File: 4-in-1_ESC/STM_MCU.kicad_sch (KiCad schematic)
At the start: 4 parts, among them U9 STM32G071GBU6

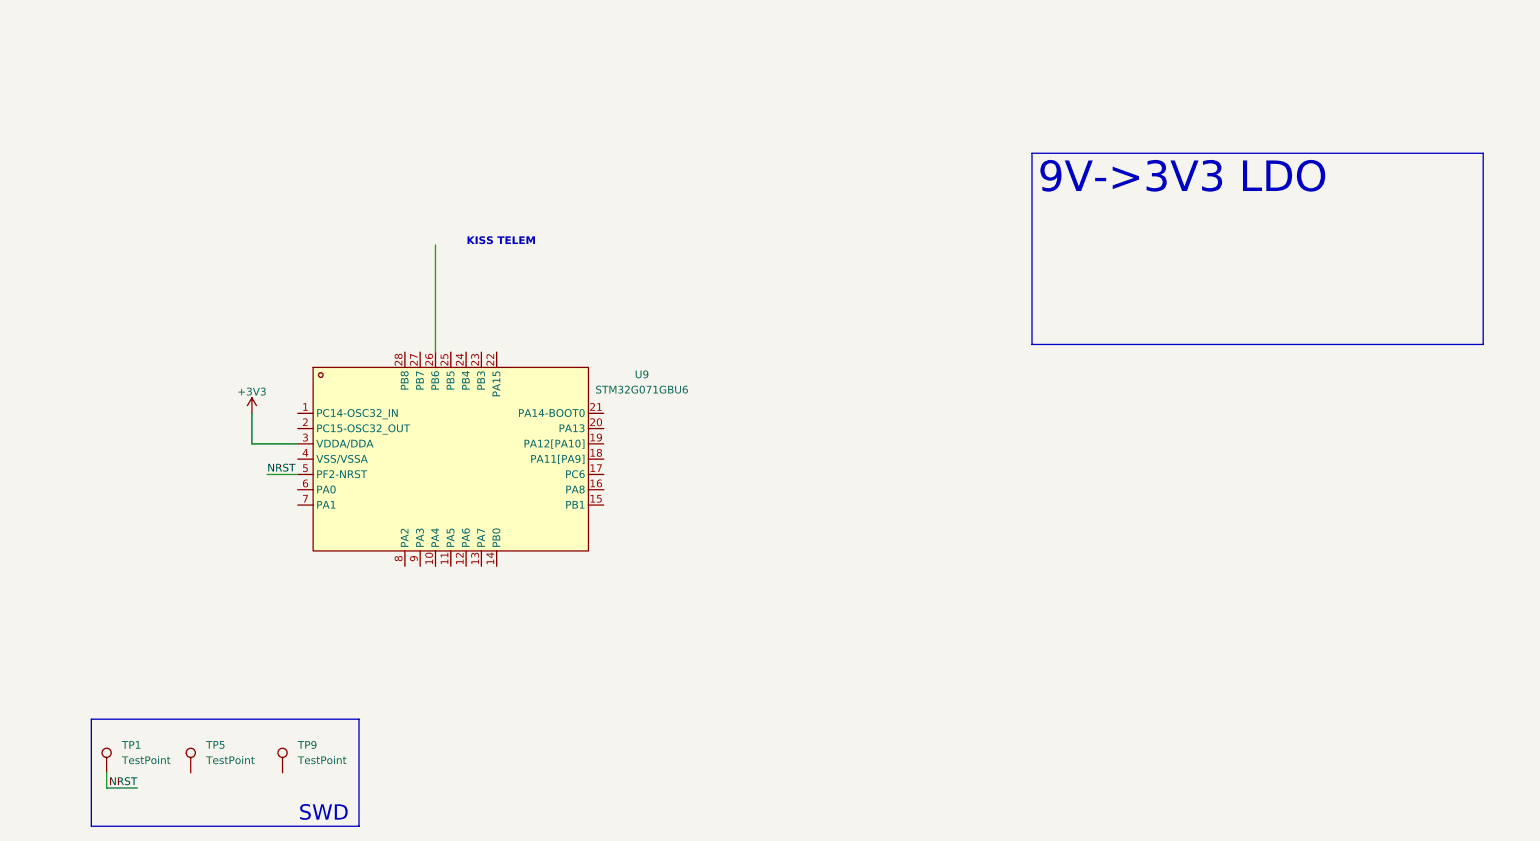
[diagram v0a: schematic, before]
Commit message: Schematic Updates
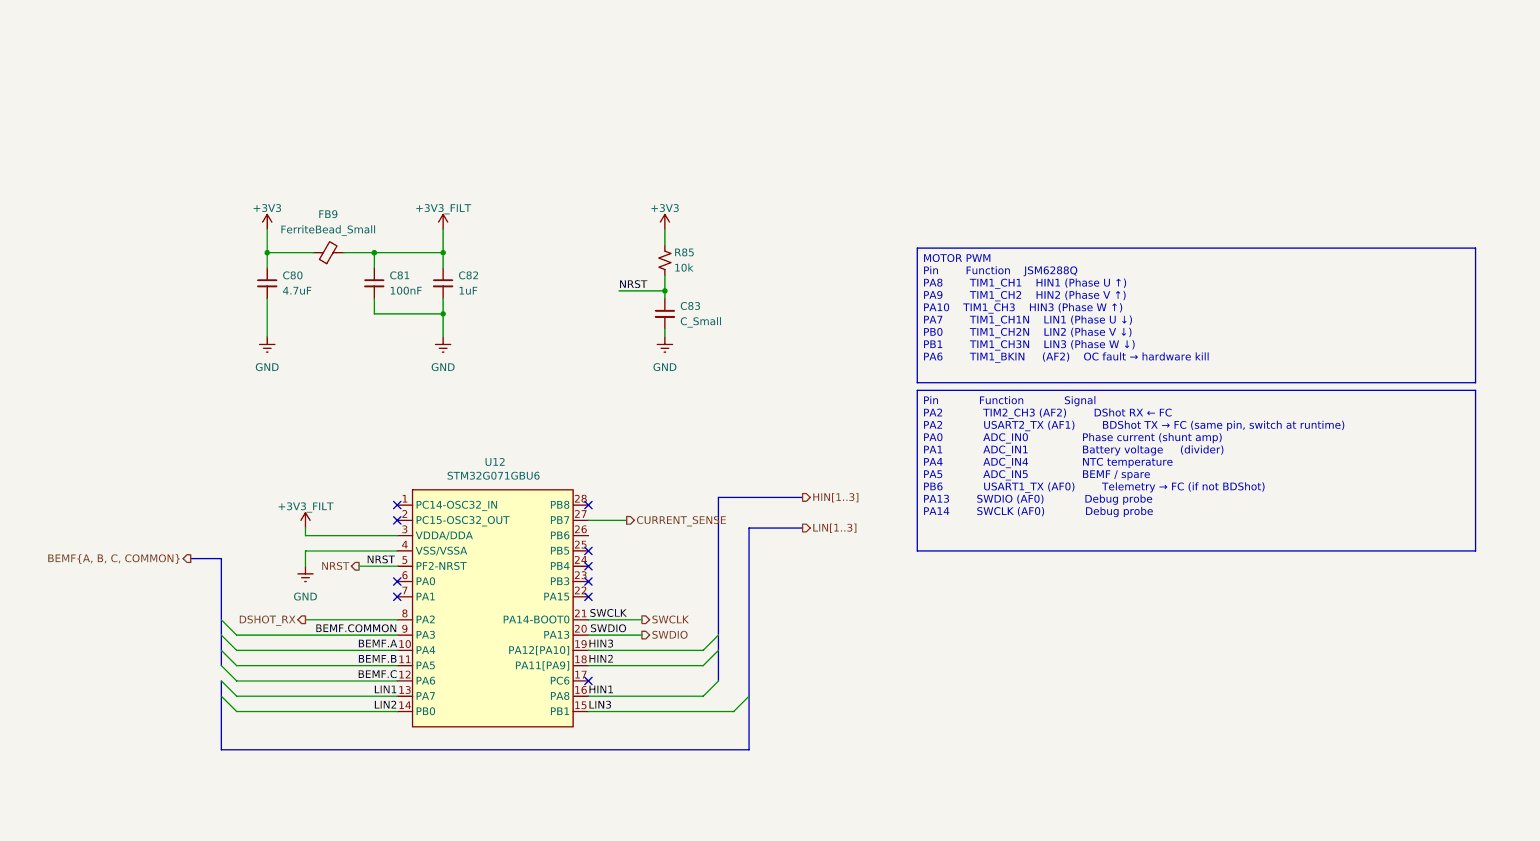
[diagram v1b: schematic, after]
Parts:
- removed TP1, TP5, TP9: TestPoint, symbol Connector:TestPoint
- added C80: 4.7uF, Capacitor_SMD:C_0402_1005Metric, symbol Device:C_Small
- added C81: 100nF, Capacitor_SMD:C_0402_1005Metric, symbol Device:C_Small
- added C82: 1uF, Capacitor_SMD:C_0402_1005Metric, symbol Device:C_Small
- added C83: C_Small, Capacitor_SMD:C_0402_1005Metric, symbol Device:C_Small
- added FB9: FerriteBead_Small, Inductor_SMD:L_0402_1005Metric, symbol Device:FerriteBead_Small
- added R85: 10k, Resistor_SMD:R_0402_1005Metric, symbol Device:R_Small_US
- renumbered U9 to U12
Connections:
- net +3V3: now also C80.1, FB9.1, R85.1; no longer U12.3 (VDDA/DDA)
- net NRST: now also C83.1, R85.2
- net BEMF.A: now reaches U12.10 (PA4)
- net BEMF.B: now reaches U12.11 (PA5)
- net BEMF.C: now reaches U12.12 (PA6)
- net LIN1: now reaches U12.13 (PA7)
- net LIN2: now reaches U12.14 (PB0)
- net LIN3: now reaches U12.15 (PB1)
- net HIN1: now reaches U12.16 (PA8)
- net HIN2: now reaches U12.18 (PA11[PA9])
- net HIN3: now reaches U12.19 (PA12[PA10])
- net SWDIO: now reaches U12.20 (PA13)
- net SWCLK: now reaches U12.21 (PA14-BOOT0)
- net CURRENT_SENSE: now reaches U12.27 (PB7)
- net GND: now reaches U12.4 (VSS/VSSA)
- net GND: now also C80.2, C81.2, C82.2, C83.2
- net DSHOT_RX: now reaches U12.8 (PA2)
- net BEMF.COMMON: now reaches U12.9 (PA3)
- new net +3V3_FILT: C81.1, C82.1, FB9.2, U12.3 (VDDA/DDA)
- no-connect marks 0 -> 10
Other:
- note removed: "KISS TELEM"
- note removed: "SWD"

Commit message: Schematic First Pass
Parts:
- removed C82: 1uF, Capacitor_SMD:C_0402_1005Metric, symbol Device:C_Small
- added C71: 100nF, Capacitor_SMD:C_0402_1005Metric, symbol Device:C_Small
- added D13: LED_Small, symbol Device:LED_Small
- added R100: 100R, Resistor_SMD:R_0402_1005Metric, symbol Device:R_Small_US
- added R104: 10k, Resistor_SMD:R_0402_1005Metric, symbol Device:R_Small_US
- added TH1: 10kΩ 3453K, symbol Device:Thermistor_NTC_US
- C83: value C_Small -> 1uF
- FB9: value FerriteBead_Small -> 600Ω@100MHz; LCSC_Part_Number (none) -> C160977
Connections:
- net +3V3: now also C71.1
- net +3V3_FILT: now also TH1.1
- net BEMF.A: now also U12.27 (PB7); no longer U12.10 (PA4)
- net BEMF.B: now also U12.23 (PB3); no longer U12.11 (PA5)
- net BEMF.C: now also U12.8 (PA2); no longer U12.12 (PA6)
- net CURRENT_SENSE: now also U12.11 (PA5); no longer U12.27 (PB7)
- net DSHOT_RX: now also U12.24 (PB4); no longer U12.8 (PA2)
- net GND: now also C71.2, D13.1 (K), R104.2
- net LED_INDICATOR: now reaches U12.17 (PC6)
- net LED_INDICATOR: now also R100.1
- net KISS_TELEM: now reaches U12.26 (PB6)
- new net: D13.2 (A), R100.2
- new net NTC_TEMP: R104.1, TH1.2, U12.10 (PA4)
- no-connect marks 10 -> 8
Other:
- note added: "3V3 INPUT FILTER"
- note added: "Arm Cortex-M0+ 32-bit MCU, up to 128 KB Flash, 36 KB RAM, 4x USART, timers, ADC, DAC, comm. I/Fs, 1.7-3.6V"
- note added: "LED INDICATOR"
- note added: "MCU"
- note added: "MOTOR TEMPERATURE READING"
- note added: "NRST PULLUP"
- note added: "STM32G071GBU6"
- moved on the sheet: C81, C83, FB9, R85, U12
